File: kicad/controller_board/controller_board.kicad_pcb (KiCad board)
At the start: 2 copper layers, 49.5 x 31 mm, 10 parts, among them J1 Battery Conn, Q1 FQP27P06, SW1 On/Off, SW2 Pair/Direction, U1 ESP32-C3-SuperMini

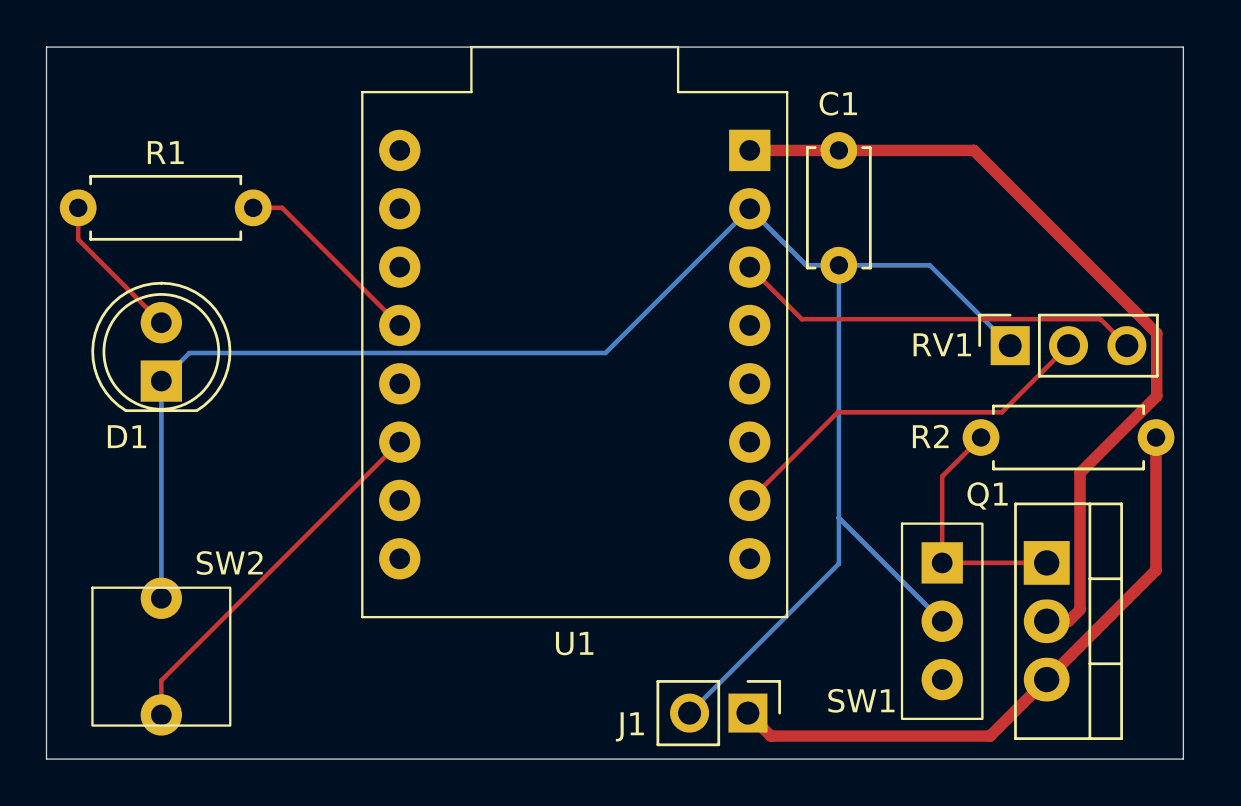
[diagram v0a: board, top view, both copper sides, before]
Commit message: Remove BMS and reorganize receiver boards for external charging
Major schematic and layout revision based on EE review:

- Remove BMS from receiver design; pivot to external LiPo charging
- Reorganize components between power and logic boards:
  - Logic board: P-FET power switch, buck converter, UI (LED/button), debug UART
  - Power board: ESP32-C3, motor driver, battery monitoring
- Add voltage dividers for 2S LiPo monitoring (B+ and BM)
  - Safe ADC voltages: B+ = 2.36V max, BM = 2.47V max
- Add debug UART headers (GPIO20/21) for serial output when USB unavailable
- Fix P-FET drain connection to properly power both buck and motor system
- Update B2B connectors to dual 6-pin configuration (signal + power)
- Minor controller board PCB layout adjustments

Co-Authored-By: Claude Sonnet 4.5 <noreply@anthropic.com>
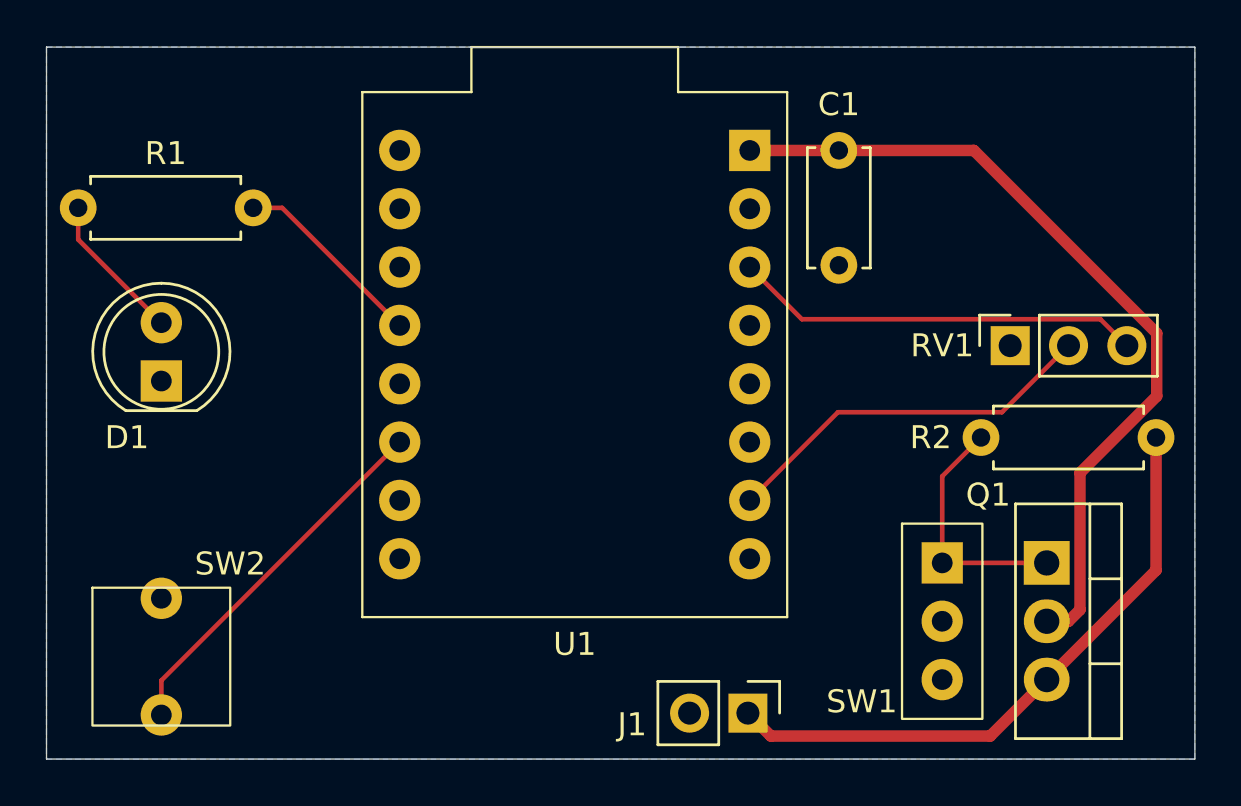
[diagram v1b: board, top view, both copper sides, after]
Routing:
- net /GND: track 80.6 -> 0.00 mm
- added copper zone on B.Cu, net /GND
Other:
- board size 49.5 x 31 mm -> 50 x 31 mm
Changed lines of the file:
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@@
 	(gr_rect
 		(start 149 65)
-		(end 198.5 96)
+		(end 199 96)
 		(stroke
 			(width 0.05)
@@
 	)
 	(segment
-		(start 183.5 74.5)
-		(end 187.46 74.5)
-		(width 0.2)
-		(layer "B.Cu")
-		(net 2)
-	)
-	(segment
-		(start 173.339 78.321)
-		(end 155.219 78.321)
-		(width 0.2)
-		(layer "B.Cu")
-		(net 2)
-	)
-	(segment
-		(start 155.219 78.321)
-		(end 154 79.54)
-		(width 0.2)
-		(layer "B.Cu")
-		(net 2)
-	)
-	(segment
-		(start 177 94)
-		(end 183.5 87.5)
-		(width 0.2)
-		(layer "B.Cu")
-		(net 2)
-	)
-	(segment
-		(start 179.62 72.04)
-		(end 182.08 74.5)
-		(width 0.2)
-		(layer "B.Cu")
-		(net 2)
-	)
-	(segment
-		(start 182.08 74.5)
-		(end 183.5 74.5)
-		(width 0.2)
-		(layer "B.Cu")
-		(net 2)
-	)
-	(segment
-		(start 183.5 85.5)
-		(end 188 90)
-		(width 0.2)
-		(layer "B.Cu")
-		(net 2)
-	)
-	(segment
-		(start 187.46 74.5)
-		(end 190.96 78)
-		(width 0.2)
-		(layer "B.Cu")
-		(net 2)
-	)
-	(segment
-		(start 183.5 87.5)
-		(end 183.5 85.5)
-		(width 0.2)
-		(layer "B.Cu")
-		(net 2)
-	)
-	(segment
-		(start 183.5 74.5)
-		(end 183.5 85.5)
-		(width 0.2)
-		(layer "B.Cu")
-		(net 2)
-	)
-	(segment
-		(start 154 79.54)
-		(end 154 89)
-		(width 0.2)
-		(layer "B.Cu")
-		(net 2)
-	)
-	(segment
-		(start 179.62 72.04)
-		(end 173.339 78.321)
-		(width 0.2)
-		(layer "B.Cu")
-		(net 2)
-	)
-	(segment
 		(start 150.38 73.38)
 		(end 154 77)
@@
 		(net 14)
 	)
+	(zone
+		(net 2)
+		(net_name "/GND")
+		(layer "B.Cu")
+		(hatch edge 0.5)
+		(connect_pads
+			(clearance 0.5)
+		)
+		(min_thickness 0.25)
+		(filled_areas_thickness no)
+		(fill yes
+			(thermal_gap 0.5)
+			(thermal_bridge_width 0.5)
+		)
+		(polygon
+			(pts
+				(xy 149 65) (xy 149 96) (xy 199 96) (xy 199 65)
+			)
+		)
+	)
 	(embedded_fonts no)
